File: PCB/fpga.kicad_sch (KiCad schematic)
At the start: 15 parts, among them U1 LFE5U-25F-6BG256x, Y1 KC2520Z

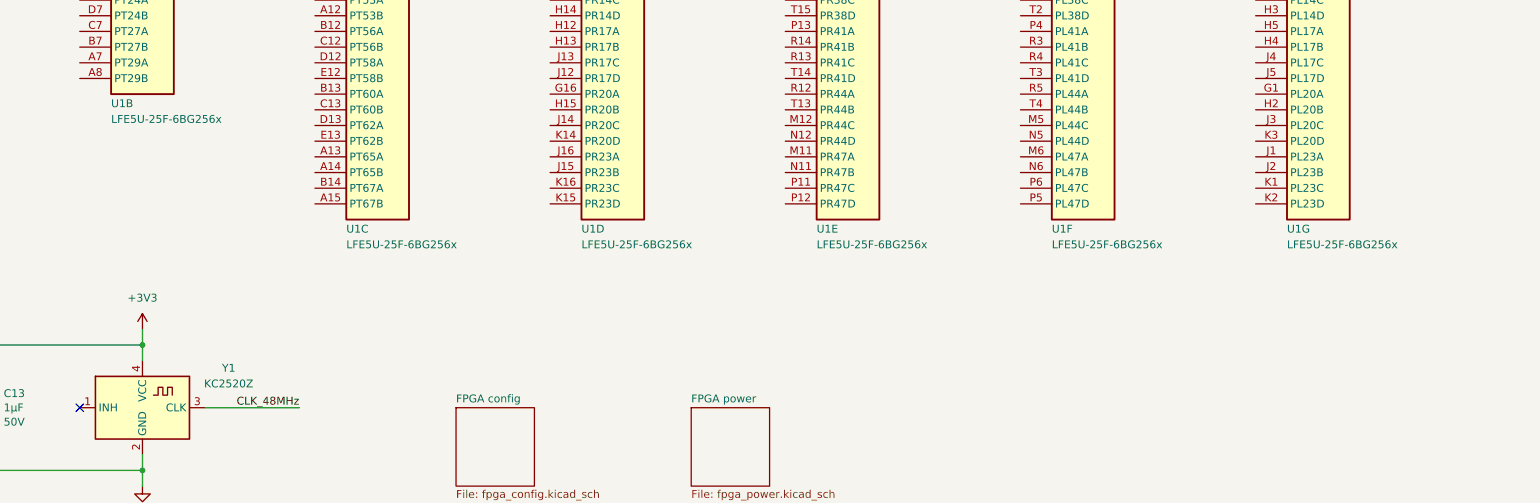
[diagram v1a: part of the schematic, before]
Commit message: Add power supplies
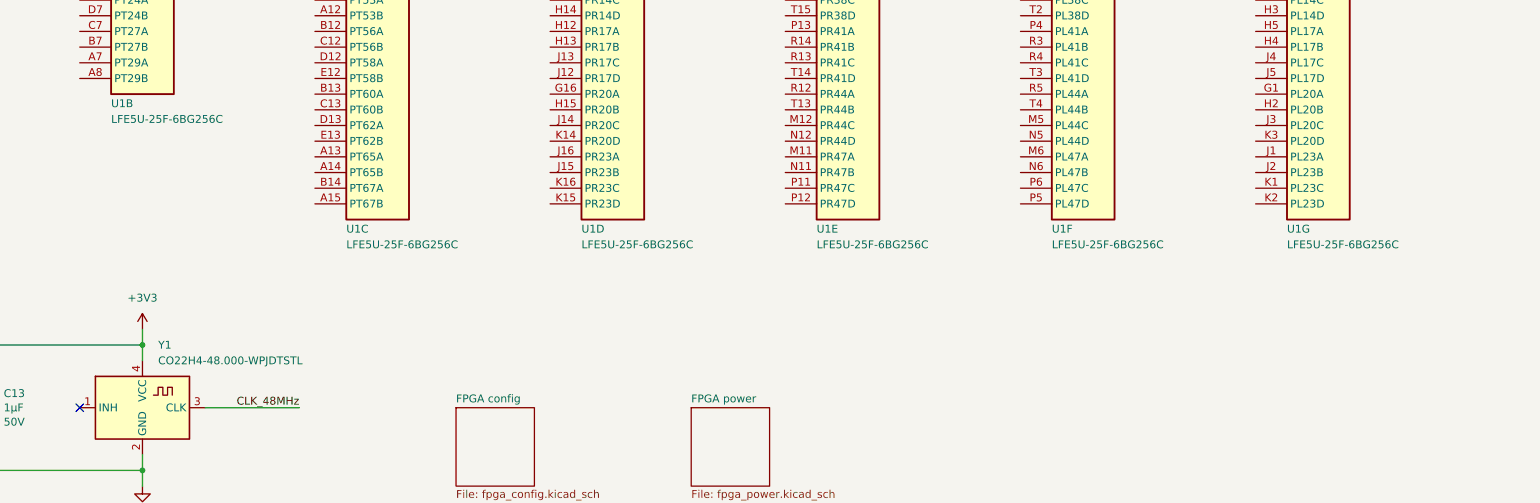
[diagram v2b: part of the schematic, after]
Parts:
- C1, C11, C13, C3, C5, C7, C9: footprint Capacitor_SMD:C_0603_1608Metric -> Capacitor_SMD:C_0402_1005Metric_Pad0.74x0.62mm_HandSolder; LCSC (none) -> C1518208; Part_number C1608X5R1H105K080AB -> GRM155R61H105KE05D
- C10, C12, C2, C4, C6, C8: footprint Capacitor_SMD:C_0603_1608Metric -> Capacitor_SMD:C_0402_1005Metric_Pad0.74x0.62mm_HandSolder; LCSC (none) -> C77020; Part_number C1608X5R1H104K080AA -> GRM155R71H104KE14D
- U1: value LFE5U-25F-6BG256x -> LFE5U-25F-6BG256C; LCSC (none) -> C1521614; Part_number (none) -> LFE5U-25F-6BG256C
- Y1: value KC2520Z -> CO22H4-48.000-WPJDTSTL; LCSC (none) -> C3034286; Part_number (none) -> CO22H4-48.000-WPJDTSTL

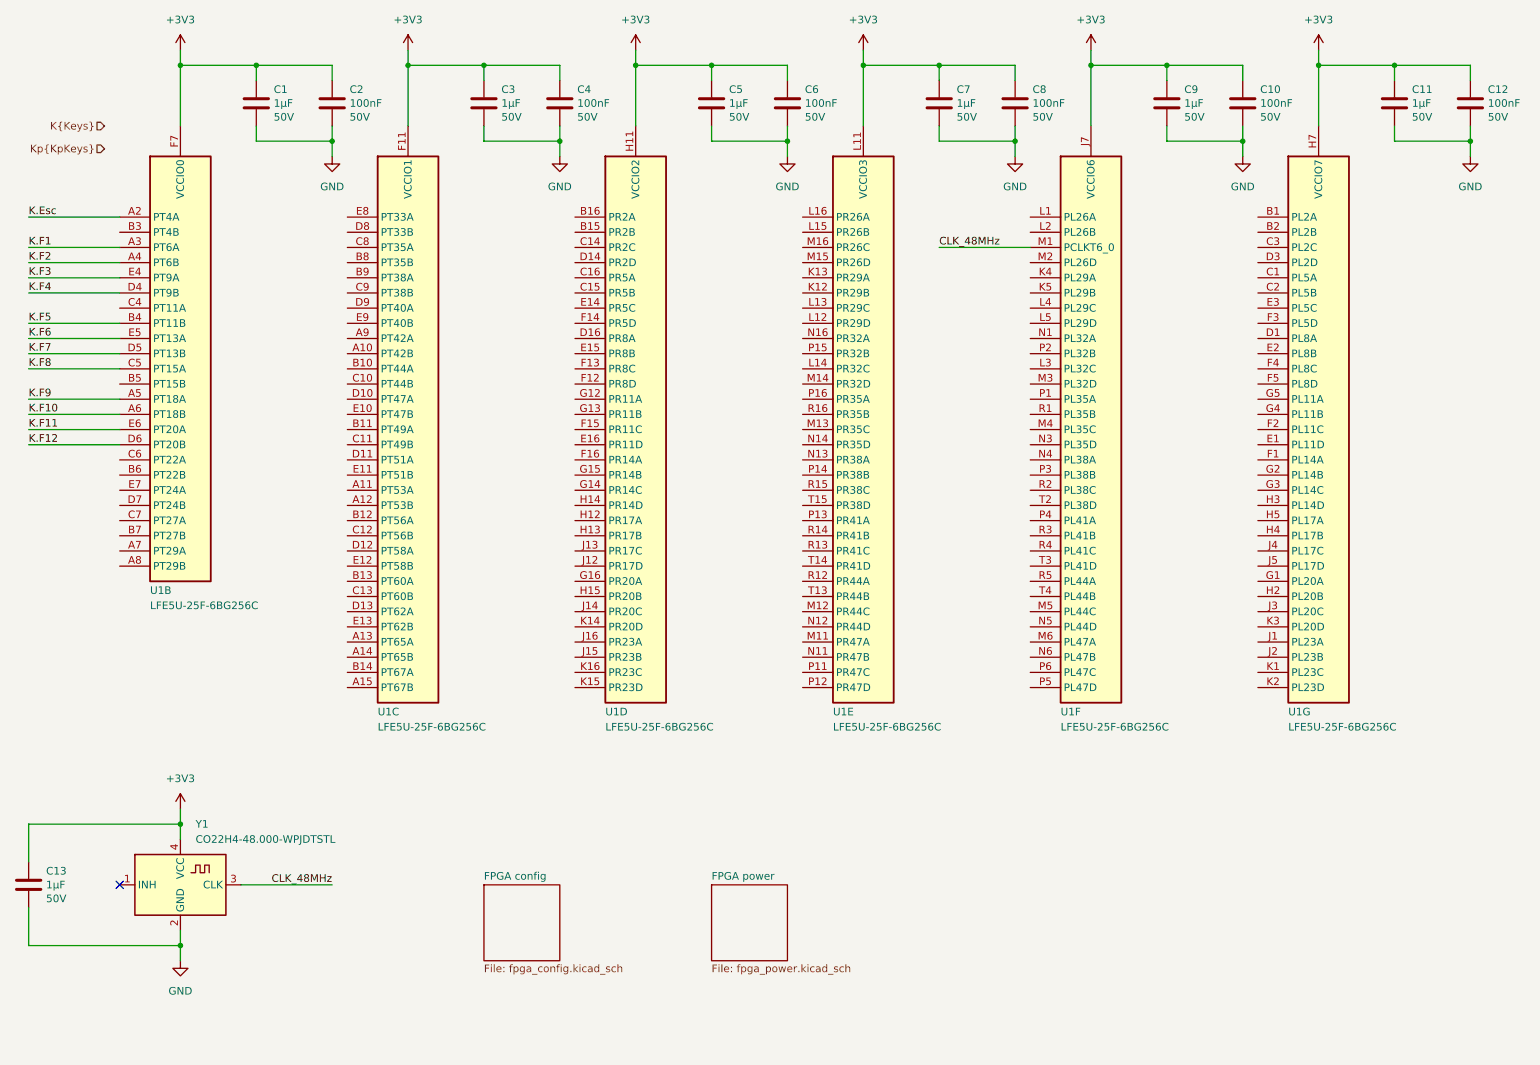
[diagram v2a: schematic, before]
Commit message: Add a USB hub
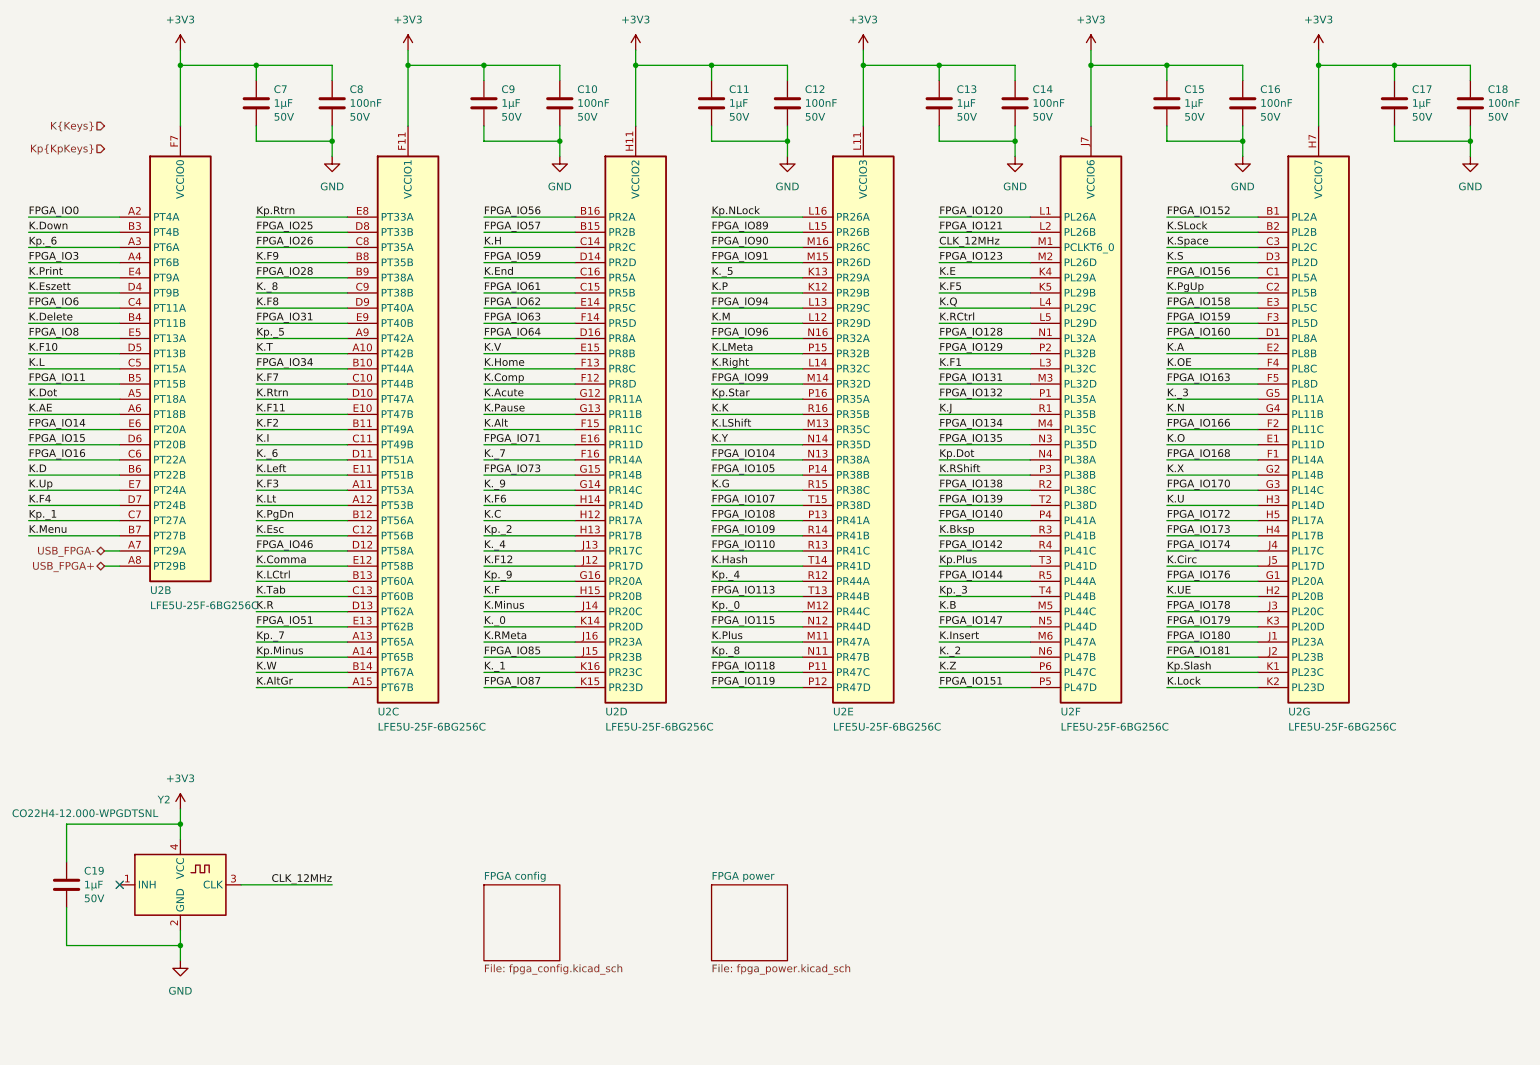
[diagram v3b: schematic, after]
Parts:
- removed Y1: CO22H4-48.000-WPJDTSTL, Oscillator:Oscillator_SMD_Kyocera_KC2520Z-4Pin_2.5x2.0mm, symbol Oscillator:KC2520Z
- added Y2: CO22H4-12.000-WPGDTSNL, Oscillator:Oscillator_SMD_Kyocera_KC2520Z-4Pin_2.5x2.0mm, symbol Oscillator:KC2520Z
- renumbered C4 to C10, C5 to C11, C6 to C12, C7 to C13, C8 to C14, C9 to C15, C10 to C16, C11 to C17, C12 to C18, C13 to C19, C1 to C7, C2 to C8, C3 to C9, U1 to U2
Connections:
- net +3V3: now also Y2.4 (VCC)
- net GND: now also Y2.2 (GND)
- net K.Esc: now also U2.C12 (PT56B); no longer U2.A2 (PT4A)
- net K.F1: now also U2.L3 (PL32C); no longer U2.A3 (PT6A)
- net K.F10: now also U2.D5 (PT13B); no longer U2.A6 (PT18B)
- net K.F11: now also U2.E10 (PT47B); no longer U2.E6 (PT20A)
- net K.F12: now also U2.J12 (PR17D); no longer U2.D6 (PT20B)
- net K.F2: now also U2.B11 (PT49A); no longer U2.A4 (PT6B)
- net K.F3: now also U2.A11 (PT53A); no longer U2.E4 (PT9A)
- net K.F4: now also U2.D7 (PT24B); no longer U2.D4 (PT9B)
- net K.F5: now also U2.K5 (PL29B); no longer U2.B4 (PT11B)
- net K.F6: now also U2.H14 (PR14D); no longer U2.E5 (PT13A)
- net K.F7: now also U2.C10 (PT44B); no longer U2.D5 (PT13B)
- net K.F8: now also U2.D9 (PT40A); no longer U2.C5 (PT15A)
- net K.F9: now also U2.B8 (PT35B); no longer U2.A5 (PT18A)
- net FPGA_IO152: now reaches U2.B1 (PL2A)
- net K.SLock: now reaches U2.B2 (PL2B)
- net FPGA_IO156: now reaches U2.C1 (PL5A)
- net K.PgUp: now reaches U2.C2 (PL5B)
- net K.Space: now reaches U2.C3 (PL2C)
- net FPGA_IO160: now reaches U2.D1 (PL8A)
- net K.S: now reaches U2.D3 (PL2D)
- net K.O: now reaches U2.E1 (PL11D)
- net K.A: now reaches U2.E2 (PL8B)
- net FPGA_IO158: now reaches U2.E3 (PL5C)
- net FPGA_IO168: now reaches U2.F1 (PL14A)
- net FPGA_IO166: now reaches U2.F2 (PL11C)
- net FPGA_IO159: now reaches U2.F3 (PL5D)
- net K.OE: now reaches U2.F4 (PL8C)
- net FPGA_IO163: now reaches U2.F5 (PL8D)
- net FPGA_IO176: now reaches U2.G1 (PL20A)
- net K.X: now reaches U2.G2 (PL14B)
- net FPGA_IO170: now reaches U2.G3 (PL14C)
- net K.N: now reaches U2.G4 (PL11B)
- net K._3: now reaches U2.G5 (PL11A)
- net K.UE: now reaches U2.H2 (PL20B)
- net K.U: now reaches U2.H3 (PL14D)
- net FPGA_IO173: now reaches U2.H4 (PL17B)
- net FPGA_IO172: now reaches U2.H5 (PL17A)
- net FPGA_IO180: now reaches U2.J1 (PL23A)
- net FPGA_IO181: now reaches U2.J2 (PL23B)
- net FPGA_IO178: now reaches U2.J3 (PL20C)
- net FPGA_IO174: now reaches U2.J4 (PL17C)
- net K.Circ: now reaches U2.J5 (PL17D)
- net Kp.Slash: now reaches U2.K1 (PL23C)
- net K.Lock: now reaches U2.K2 (PL23D)
- net FPGA_IO179: now reaches U2.K3 (PL20D)
- net K.E: now reaches U2.K4 (PL29A)
- net FPGA_IO120: now reaches U2.L1 (PL26A)
- net FPGA_IO121: now reaches U2.L2 (PL26B)
- net K.Q: now reaches U2.L4 (PL29C)
- net K.RCtrl: now reaches U2.L5 (PL29D)
- net FPGA_IO123: now reaches U2.M2 (PL26D)
- net FPGA_IO131: now reaches U2.M3 (PL32D)
- net FPGA_IO134: now reaches U2.M4 (PL35C)
- net K.B: now reaches U2.M5 (PL44C)
- net K.Insert: now reaches U2.M6 (PL47A)
- net FPGA_IO128: now reaches U2.N1 (PL32A)
- net FPGA_IO135: now reaches U2.N3 (PL35D)
- net Kp.Dot: now reaches U2.N4 (PL38A)
- net FPGA_IO147: now reaches U2.N5 (PL44D)
- net K._2: now reaches U2.N6 (PL47B)
- net FPGA_IO132: now reaches U2.P1 (PL35A)
- net FPGA_IO129: now reaches U2.P2 (PL32B)
- net K.RShift: now reaches U2.P3 (PL38B)
- net FPGA_IO140: now reaches U2.P4 (PL41A)
- net FPGA_IO151: now reaches U2.P5 (PL47D)
- net K.Z: now reaches U2.P6 (PL47C)
- net K.J: now reaches U2.R1 (PL35B)
- net FPGA_IO138: now reaches U2.R2 (PL38C)
- net K.Bksp: now reaches U2.R3 (PL41B)
- net FPGA_IO142: now reaches U2.R4 (PL41C)
- net FPGA_IO144: now reaches U2.R5 (PL44A)
- net FPGA_IO139: now reaches U2.T2 (PL38D)
- net Kp.Plus: now reaches U2.T3 (PL41D)
- net Kp._3: now reaches U2.T4 (PL44B)
- net USB_FPGA-: now reaches U2.A7 (PT29A)
- net USB_FPGA+: now reaches U2.A8 (PT29B)
- net K.Down: now reaches U2.B3 (PT4B)
- net FPGA_IO11: now reaches U2.B5 (PT15B)
- net K.D: now reaches U2.B6 (PT22B)
- net K.Menu: now reaches U2.B7 (PT27B)
- net FPGA_IO6: now reaches U2.C4 (PT11A)
- net FPGA_IO16: now reaches U2.C6 (PT22A)
- net Kp._1: now reaches U2.C7 (PT27A)
- net K.Up: now reaches U2.E7 (PT24A)
- net FPGA_IO57: now reaches U2.B15 (PR2B)
- net FPGA_IO56: now reaches U2.B16 (PR2A)
- net K.H: now reaches U2.C14 (PR2C)
- net FPGA_IO61: now reaches U2.C15 (PR5B)
- net K.End: now reaches U2.C16 (PR5A)
- net FPGA_IO59: now reaches U2.D14 (PR2D)
- net FPGA_IO64: now reaches U2.D16 (PR8A)
- net FPGA_IO62: now reaches U2.E14 (PR5C)
- net K.V: now reaches U2.E15 (PR8B)
- net FPGA_IO71: now reaches U2.E16 (PR11D)
- net K.Comp: now reaches U2.F12 (PR8D)
- net K.Home: now reaches U2.F13 (PR8C)
- net FPGA_IO63: now reaches U2.F14 (PR5D)
- net K.Alt: now reaches U2.F15 (PR11C)
- net K._7: now reaches U2.F16 (PR14A)
- net K.Acute: now reaches U2.G12 (PR11A)
- net K.Pause: now reaches U2.G13 (PR11B)
- net K._9: now reaches U2.G14 (PR14C)
- net FPGA_IO73: now reaches U2.G15 (PR14B)
- net Kp._9: now reaches U2.G16 (PR20A)
- net K.C: now reaches U2.H12 (PR17A)
- net Kp._2: now reaches U2.H13 (PR17B)
- net K.F: now reaches U2.H15 (PR20B)
- net K._4: now reaches U2.J13 (PR17C)
- net K.Minus: now reaches U2.J14 (PR20C)
- net FPGA_IO85: now reaches U2.J15 (PR23B)
- net K.RMeta: now reaches U2.J16 (PR23A)
- net K._0: now reaches U2.K14 (PR20D)
- net FPGA_IO87: now reaches U2.K15 (PR23D)
- net K._1: now reaches U2.K16 (PR23C)
- net K.T: now reaches U2.A10 (PT42B)
- net K.Lt: now reaches U2.A12 (PT53B)
- net Kp._7: now reaches U2.A13 (PT65A)
- net Kp.Minus: now reaches U2.A14 (PT65B)
- net K.AltGr: now reaches U2.A15 (PT67B)
- net Kp._5: now reaches U2.A9 (PT42A)
- net FPGA_IO34: now reaches U2.B10 (PT44A)
- net K.PgDn: now reaches U2.B12 (PT56A)
- net K.LCtrl: now reaches U2.B13 (PT60A)
- net K.W: now reaches U2.B14 (PT67A)
- net FPGA_IO28: now reaches U2.B9 (PT38A)
- net K.I: now reaches U2.C11 (PT49B)
- net K.Tab: now reaches U2.C13 (PT60B)
- net FPGA_IO26: now reaches U2.C8 (PT35A)
- net K._8: now reaches U2.C9 (PT38B)
- net K.Rtrn: now reaches U2.D10 (PT47A)
- net K._6: now reaches U2.D11 (PT51A)
- net FPGA_IO46: now reaches U2.D12 (PT58A)
- net K.R: now reaches U2.D13 (PT62A)
- net FPGA_IO25: now reaches U2.D8 (PT33B)
- net K.Left: now reaches U2.E11 (PT51B)
- net K.Comma: now reaches U2.E12 (PT58B)
- net FPGA_IO51: now reaches U2.E13 (PT62B)
- net Kp.Rtrn: now reaches U2.E8 (PT33A)
- net FPGA_IO31: now reaches U2.E9 (PT40B)
- net K.P: now reaches U2.K12 (PR29B)
- net K._5: now reaches U2.K13 (PR29A)
- net K.M: now reaches U2.L12 (PR29D)
- net FPGA_IO94: now reaches U2.L13 (PR29C)
- net K.Right: now reaches U2.L14 (PR32C)
- net FPGA_IO89: now reaches U2.L15 (PR26B)
- net Kp.NLock: now reaches U2.L16 (PR26A)
- net K.Plus: now reaches U2.M11 (PR47A)
- net Kp._0: now reaches U2.M12 (PR44C)
- net K.LShift: now reaches U2.M13 (PR35C)
- net FPGA_IO99: now reaches U2.M14 (PR32D)
- net FPGA_IO91: now reaches U2.M15 (PR26D)
- net FPGA_IO90: now reaches U2.M16 (PR26C)
- net Kp._8: now reaches U2.N11 (PR47B)
- net FPGA_IO115: now reaches U2.N12 (PR44D)
- net FPGA_IO104: now reaches U2.N13 (PR38A)
- net K.Y: now reaches U2.N14 (PR35D)
- net FPGA_IO96: now reaches U2.N16 (PR32A)
- net FPGA_IO118: now reaches U2.P11 (PR47C)
- net FPGA_IO119: now reaches U2.P12 (PR47D)
- net FPGA_IO108: now reaches U2.P13 (PR41A)
- net FPGA_IO105: now reaches U2.P14 (PR38B)
- net K.LMeta: now reaches U2.P15 (PR32B)
- net Kp.Star: now reaches U2.P16 (PR35A)
- net Kp._4: now reaches U2.R12 (PR44A)
- net FPGA_IO110: now reaches U2.R13 (PR41C)
- net FPGA_IO109: now reaches U2.R14 (PR41B)
- net K.G: now reaches U2.R15 (PR38C)
- net K.K: now reaches U2.R16 (PR35B)
- net FPGA_IO113: now reaches U2.T13 (PR44B)
- net K.Hash: now reaches U2.T14 (PR41D)
- net FPGA_IO107: now reaches U2.T15 (PR38D)
- net CLK_48MHz renamed CLK_12MHz
- net CLK_12MHz: now also Y2.3 (CLK)
- new net FPGA_IO0: U2.A2 (PT4A)
- new net FPGA_IO14: U2.E6 (PT20A)
- new net FPGA_IO15: U2.D6 (PT20B)
- new net FPGA_IO3: U2.A4 (PT6B)
- new net FPGA_IO8: U2.E5 (PT13A)
- new net K.AE: U2.A6 (PT18B)
- new net K.Delete: U2.B4 (PT11B)
- new net K.Dot: U2.A5 (PT18A)
- new net K.Eszett: U2.D4 (PT9B)
- new net K.L: U2.C5 (PT15A)
- new net K.Print: U2.E4 (PT9A)
- new net Kp._6: U2.A3 (PT6A)
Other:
- moved on the sheet: C19

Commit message: Add the USB to JTAG bridge
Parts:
- Y3: renamed from Y2; value CO22H4-12.000-WPGDTSNL -> 12MHz; footprint Oscillator:Oscillator_SMD_Kyocera_KC2520Z-4Pin_2.5x2.0mm -> Crystal:Crystal_SMD_2520-4Pin_2.5x2.0mm
- renumbered C7 to C12, C8 to C13, C9 to C14, C10 to C15, C11 to C16, C12 to C17, C13 to C18, C14 to C19, C15 to C20, C16 to C21, C17 to C22, C18 to C23, C19 to C24, U2 to U3

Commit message: Improve the CH347F schematics and added 3D models
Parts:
- added J8: Pin header, 2x4, Connector_PinHeader_2.54mm:PinHeader_2x04_P2.54mm_Vertical, symbol Connector_Generic:Conn_02x04_Counter_Clockwise
- renumbered U3 to U4
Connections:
- net FPGA_IO118: now also J8.1 (Pin_1)
- net FPGA_IO119: now also J8.2 (Pin_2)
- net FPGA_IO180: now also J8.3 (Pin_3)
- net FPGA_IO181: now also J8.4 (Pin_4)
- net FPGA_IO46: now also J8.5 (Pin_5)
- net FPGA_IO51: now also J8.6 (Pin_6)
- net FPGA_IO85: now also J8.7 (Pin_7)
- net FPGA_IO87: now also J8.8 (Pin_8)

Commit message: Add LICENSE and minor improvements
- Filled the title blocks
- Connected the LEDs to the FPGA
- Changed the FPGA programming header
- Added USB fuse and capacitors
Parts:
- added J9: Pin header, 2x4, Connector_PinHeader_2.54mm:PinHeader_2x04_P2.54mm_Vertical, symbol Connector_Generic:Conn_02x04_Counter_Clockwise
- renumbered C12 to C14, C13 to C15, C14 to C16, C15 to C17, C16 to C18, C17 to C19, C18 to C20, C19 to C21, C20 to C22, C21 to C23, C22 to C24, C23 to C25, C24 to C26
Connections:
- net FPGA_IO131: now also J9.8 (Pin_8)
- net FPGA_IO132: now also J9.7 (Pin_7)
- net FPGA_IO134: now also J9.6 (Pin_6)
- net FPGA_IO135: now also J9.5 (Pin_5)
- net FPGA_IO172: now also J9.1 (Pin_1)
- net FPGA_IO173: now also J9.2 (Pin_2)
- net FPGA_IO174: now also J9.3 (Pin_3)
- net FPGA_IO176: now also J9.4 (Pin_4)
- net FPGA_IO61 renamed LED0
- net FPGA_IO62 renamed LED1
- net FPGA_IO63 renamed LED2
- net FPGA_IO64 renamed LED3
- net FPGA_IO71 renamed LED4
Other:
- company: (none) -> Copyright (c) 2025 L. Sartory
- title: (none) -> Clavier - FPGA

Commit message: Place and route peripheral components
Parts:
- removed J8, J9: Pin header, 2x4, Connector_PinHeader_2.54mm:PinHeader_2x04_P2.54mm_Vertical, symbol Connector_Generic:Conn_02x04_Counter_Clockwise
- added J8, J9: Pin header, 2x4, Connector_PinHeader_2.54mm:PinHeader_2x04_P2.54mm_Vertical, symbol Connector_Generic:Conn_02x04_Odd_Even
- added R16: 1.5kΩ, Resistor_SMD:R_0402_1005Metric_Pad0.72x0.64mm_HandSolder, symbol Device:R
- renumbered C14 to C17, C15 to C18, C16 to C19, C17 to C20, C18 to C21, C19 to C22, C20 to C23, C21 to C24, C22 to C25, C23 to C26, C24 to C27, C25 to C28, C26 to C29
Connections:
- net FPGA_IO156 is gone; now on net USB_FPGA+: U4.C1 (PL5A)
- net FPGA_IO160 is gone; now on net USB_FPGA-: U4.D1 (PL8A)
- net FPGA_IO118: now also J8.1 (Pin_1)
- net FPGA_IO119: now also J8.3 (Pin_3)
- net FPGA_IO131: now also J9.2 (Pin_2)
- net FPGA_IO132: now also J9.4 (Pin_4)
- net FPGA_IO134: now also J9.6 (Pin_6)
- net FPGA_IO135: now also J9.8 (Pin_8)
- net FPGA_IO172: now also J9.1 (Pin_1)
- net FPGA_IO173: now also J9.3 (Pin_3)
- net FPGA_IO174: now also J9.5 (Pin_5)
- net FPGA_IO176: now also J9.7 (Pin_7)
- net FPGA_IO180: now also J8.5 (Pin_5)
- net FPGA_IO181: now also J8.7 (Pin_7)
- net FPGA_IO46: now also J8.8 (Pin_8)
- net FPGA_IO51: now also J8.6 (Pin_6)
- net FPGA_IO85: now also J8.4 (Pin_4)
- net FPGA_IO87: now also J8.2 (Pin_2)
- net USB_FPGA+: now also R16.2; no longer U4.A8 (PT29B)
- net USB_FPGA-: no longer U4.A7 (PT29A)
- net FPGA_IO152 renamed USB_Pull_Up
- net USB_Pull_Up: now also R16.1
- new net FPGA_IO315: U4.A7 (PT29A)
- new net FPGA_IO316: U4.A8 (PT29B)
